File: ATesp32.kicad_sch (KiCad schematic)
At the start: 28 parts, among them SW1 SW_Push, SW2 SW_Push, U1 ESP32-S3, U2 ATmega32A-P, Y1 40 MHz

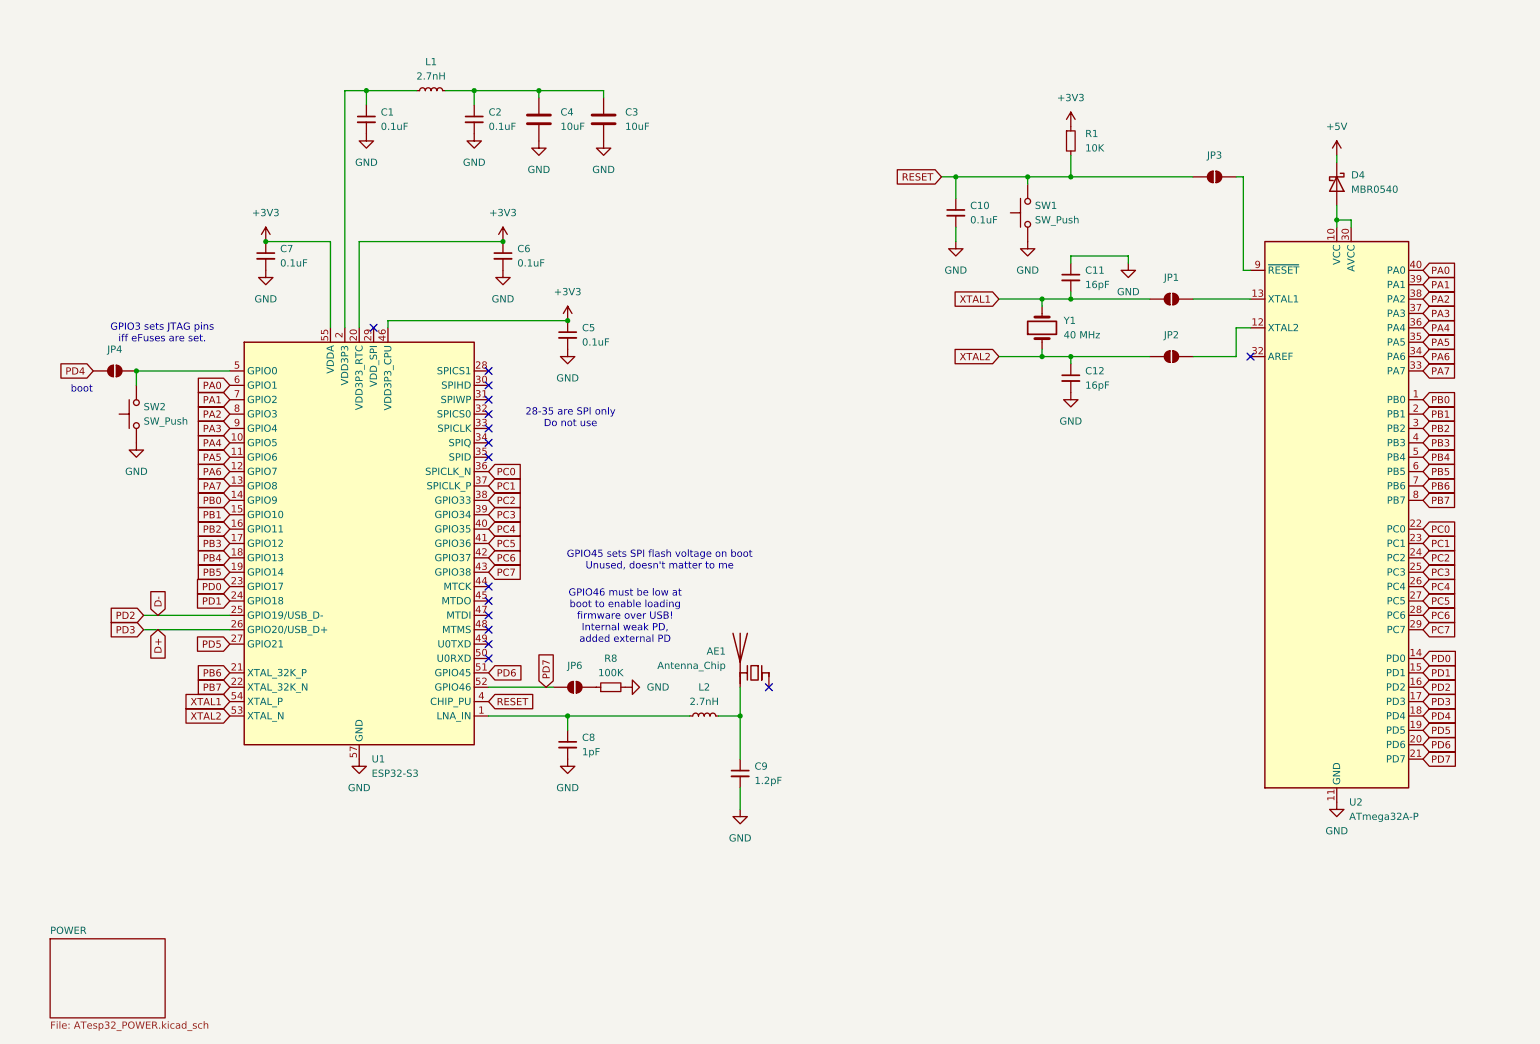
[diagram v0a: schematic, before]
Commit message: Added USB-UART bridge for programming
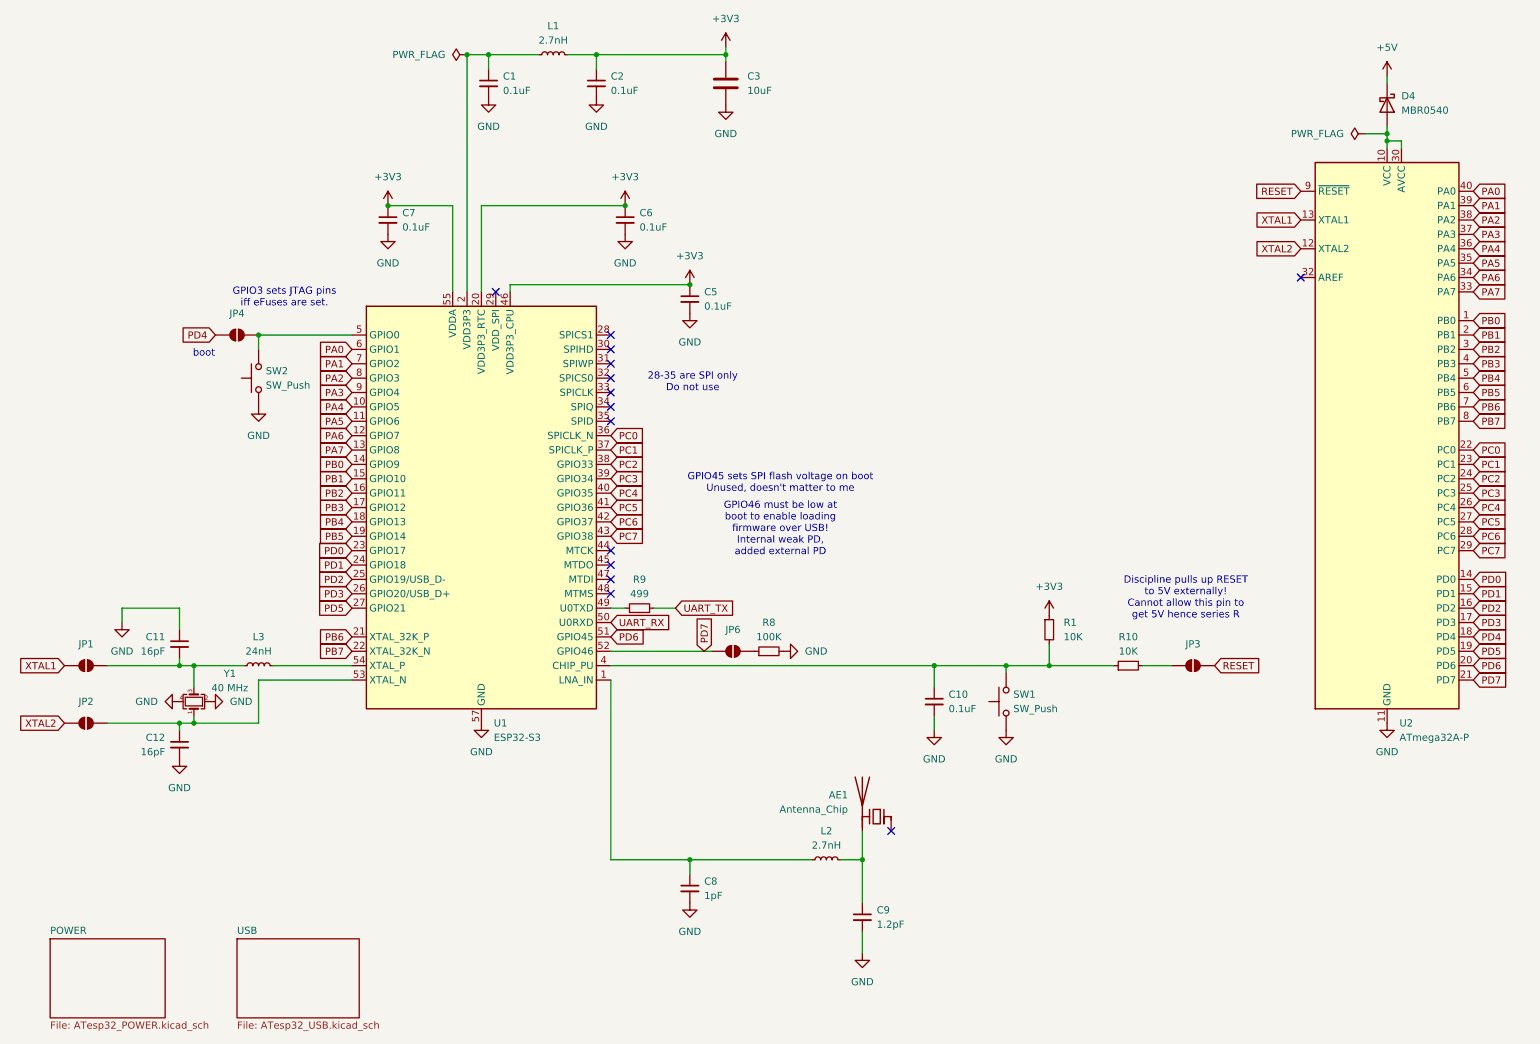
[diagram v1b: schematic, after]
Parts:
- removed C4: 10uF, symbol Device:C
- removed Y1: 40 MHz, symbol Device:Crystal
- added L3: 24nH, symbol Device:L_Small
- added R10: 10K, symbol Device:R_Small
- added R9: 499, symbol Device:R_Small
- added Y1: 40 MHz, symbol Device:Crystal_GND24_Small
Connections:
- net +3V3: now also C2.1, C3.1, L1.2
- net GND: now also Y1.2, Y1.4
- net RESET: now also JP3.2 (B), U2.9 (~{RESET}); no longer C10.1, JP3.1 (A), R1.2, SW1.2, U1.4 (CHIP_PU)
- net XTAL1: now also JP1.2 (B), U2.13 (XTAL1); no longer C11.2, JP1.1 (A), U1.54 (XTAL_P)
- net XTAL2: now also JP2.2 (B), U2.12 (XTAL2); no longer C12.1, JP2.1 (A), U1.53 (XTAL_N)
- net at U1.49 (U0TXD): now also R9.1
- net UART_RX: now reaches U1.50 (U0RXD)
- net D+ renamed PD3
- net D- renamed PD2
- new net: C12.1, JP2.1 (A), U1.53 (XTAL_N), Y1.1
- new net: C11.2, JP1.1 (A), L3.1, Y1.3
- new net: C10.1, R1.2, R10.1, SW1.2, U1.4 (CHIP_PU)
- new net: L3.2, U1.54 (XTAL_P)
- new net: JP3.1 (A), R10.2
- new net UART_TX: R9.2
- no-connect marks 16 -> 14
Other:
- added sheet USB (ATesp32_USB.kicad_sch)
- note added: "Discipline pulls up RESET to 5V externally! Cannot allow this pin to get 5V hence series R"
- moved on the sheet: AE1, C1, C10, C11, C12, C2, C3, C5, C6, C7, C8, C9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

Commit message: first pass at footprint assignment
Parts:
- AE1: footprint (none) -> RF_Antenna:Johanson_2450AT18x100
- C1, C10, C11, C12, C2, C3, C5, C6, C7, C8, C9: footprint (none) -> Capacitor_SMD:C_0603_1608Metric
- JP1, JP2, JP3, JP4, JP6: footprint (none) -> Jumper:SolderJumper-2_P1.3mm_Open_RoundedPad1.0x1.5mm
- L1, L2, L3: footprint (none) -> Inductor_SMD:L_0603_1608Metric
- R1, R10, R8, R9: footprint (none) -> Resistor_SMD:R_0603_1608Metric
- SW1, SW2: footprint (none) -> Button_Switch_SMD:SW_Push_1P1T_NO_CK_KMR2
- Y1: footprint (none) -> Crystal:Crystal_SMD_Abracon_ABM8G-4Pin_3.2x2.5mm
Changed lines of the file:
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@@
 			)
 		)
-		(property "Footprint" ""
+		(property "Footprint" "Capacitor_SMD:C_0603_1608Metric"
 			(at 135.89 63.5 0)
 			(effects
@@
 			)
 		)
-		(property "Footprint" ""
+		(property "Footprint" "RF_Antenna:Johanson_2450AT18x100"
 			(at 171.45 150.495 0)
 			(effects
@@
 			)
 		)
-		(property "Footprint" ""
+		(property "Footprint" "Crystal:Crystal_SMD_Abracon_ABM8G-4Pin_3.2x2.5mm"
 			(at 48.26 134.62 0)
 			(effects
@@
 			)
 		)
-		(property "Footprint" ""
+		(property "Footprint" "Jumper:SolderJumper-2_P1.3mm_Open_RoundedPad1.0x1.5mm"
 			(at 29.21 138.43 0)
 			(effects
@@
 			)
 		)
-		(property "Footprint" ""
+		(property "Footprint" "Capacitor_SMD:C_0603_1608Metric"
 			(at 119.38 25.4 0)
 			(effects
@@
 			)
 		)
-		(property "Footprint" ""
+		(property "Footprint" "Jumper:SolderJumper-2_P1.3mm_Open_RoundedPad1.0x1.5mm"
 			(at 29.21 128.27 0)
 			(effects
@@
 			)
 		)
-		(property "Footprint" ""
+		(property "Footprint" "Jumper:SolderJumper-2_P1.3mm_Open_RoundedPad1.0x1.5mm"
 			(at 143.51 125.73 0)
 			(effects
@@
 			)
 		)
-		(property "Footprint" ""
+		(property "Footprint" "Capacitor_SMD:C_0603_1608Metric"
 			(at 45.72 124.46 0)
 			(effects
@@
 			)
 		)
-		(property "Footprint" ""
+		(property "Footprint" "Capacitor_SMD:C_0603_1608Metric"
 			(at 166.37 172.72 0)
 			(effects
@@
 			)
 		)
-		(property "Footprint" ""
+		(property "Footprint" "Inductor_SMD:L_0603_1608Metric"
 			(at 111.76 20.32 0)
 			(effects
@@
 			)
 		)
-		(property "Footprint" ""
+		(property "Footprint" "Jumper:SolderJumper-2_P1.3mm_Open_RoundedPad1.0x1.5mm"
 			(at 224.79 128.27 0)
 			(effects
@@
 			)
 		)
-		(property "Footprint" ""
+		(property "Footprint" "Capacitor_SMD:C_0603_1608Metric"
 			(at 143.2052 29.21 0)
 			(effects
@@
 			)
 		)
-		(property "Footprint" ""
+		(property "Footprint" "Capacitor_SMD:C_0603_1608Metric"
 			(at 124.46 49.53 0)
 			(effects
@@
 			)
 		)
-		(property "Footprint" ""
+		(property "Footprint" "Capacitor_SMD:C_0603_1608Metric"
 			(at 100.33 25.4 0)
 			(effects
@@
 			)
 		)
-		(property "Footprint" ""
+		(property "Footprint" "Jumper:SolderJumper-2_P1.3mm_Open_RoundedPad1.0x1.5mm"
 			(at 55.88 69.85 0)
 			(effects
@@
 			)
 		)
-		(property "Footprint" ""
+		(property "Footprint" "Button_Switch_SMD:SW_Push_1P1T_NO_CK_KMR2"
 			(at 186.69 134.62 0)
 			(effects
@@
 			)
 		)
-		(property "Footprint" ""
+		(property "Footprint" "Capacitor_SMD:C_0603_1608Metric"
 			(at 82.55 49.53 0)
 			(effects
@@
 			)
 		)
-		(property "Footprint" ""
+		(property "Footprint" "Capacitor_SMD:C_0603_1608Metric"
 			(at 135.89 167.64 0)
 			(effects
@@
 			)
 		)
-		(property "Footprint" ""
+		(property "Footprint" "Resistor_SMD:R_0603_1608Metric"
 			(at 213.36 128.27 0)
 			(effects
@@
 			)
 		)
-		(property "Footprint" ""
+		(property "Footprint" "Capacitor_SMD:C_0603_1608Metric"
 			(at 45.72 142.24 0)
 			(effects
@@
 			)
 		)
-		(property "Footprint" ""
+		(property "Footprint" "Inductor_SMD:L_0603_1608Metric"
 			(at 59.69 128.27 0)
 			(effects
@@
 			)
 		)
-		(property "Footprint" ""
+		(property "Footprint" "Resistor_SMD:R_0603_1608Metric"
 			(at 149.86 125.73 0)
 			(effects
@@
 			)
 		)
-		(property "Footprint" ""
+		(property "Footprint" "Resistor_SMD:R_0603_1608Metric"
 			(at 127 118.11 0)
 			(effects
@@
 			)
 		)
-		(property "Footprint" ""
+		(property "Footprint" "Resistor_SMD:R_0603_1608Metric"
 			(at 199.39 121.92 0)
 			(effects
@@
 			)
 		)
-		(property "Footprint" ""
+		(property "Footprint" "Button_Switch_SMD:SW_Push_1P1T_NO_CK_KMR2"
 			(at 54.61 77.47 0)
 			(effects
@@
 			)
 		)
-		(property "Footprint" ""
+		(property "Footprint" "Capacitor_SMD:C_0603_1608Metric"
 			(at 179.07 134.62 0)
 			(effects
@@
 			)
 		)
-		(property "Footprint" ""
+		(property "Footprint" "Inductor_SMD:L_0603_1608Metric"
 			(at 160.02 162.56 0)
 			(effects

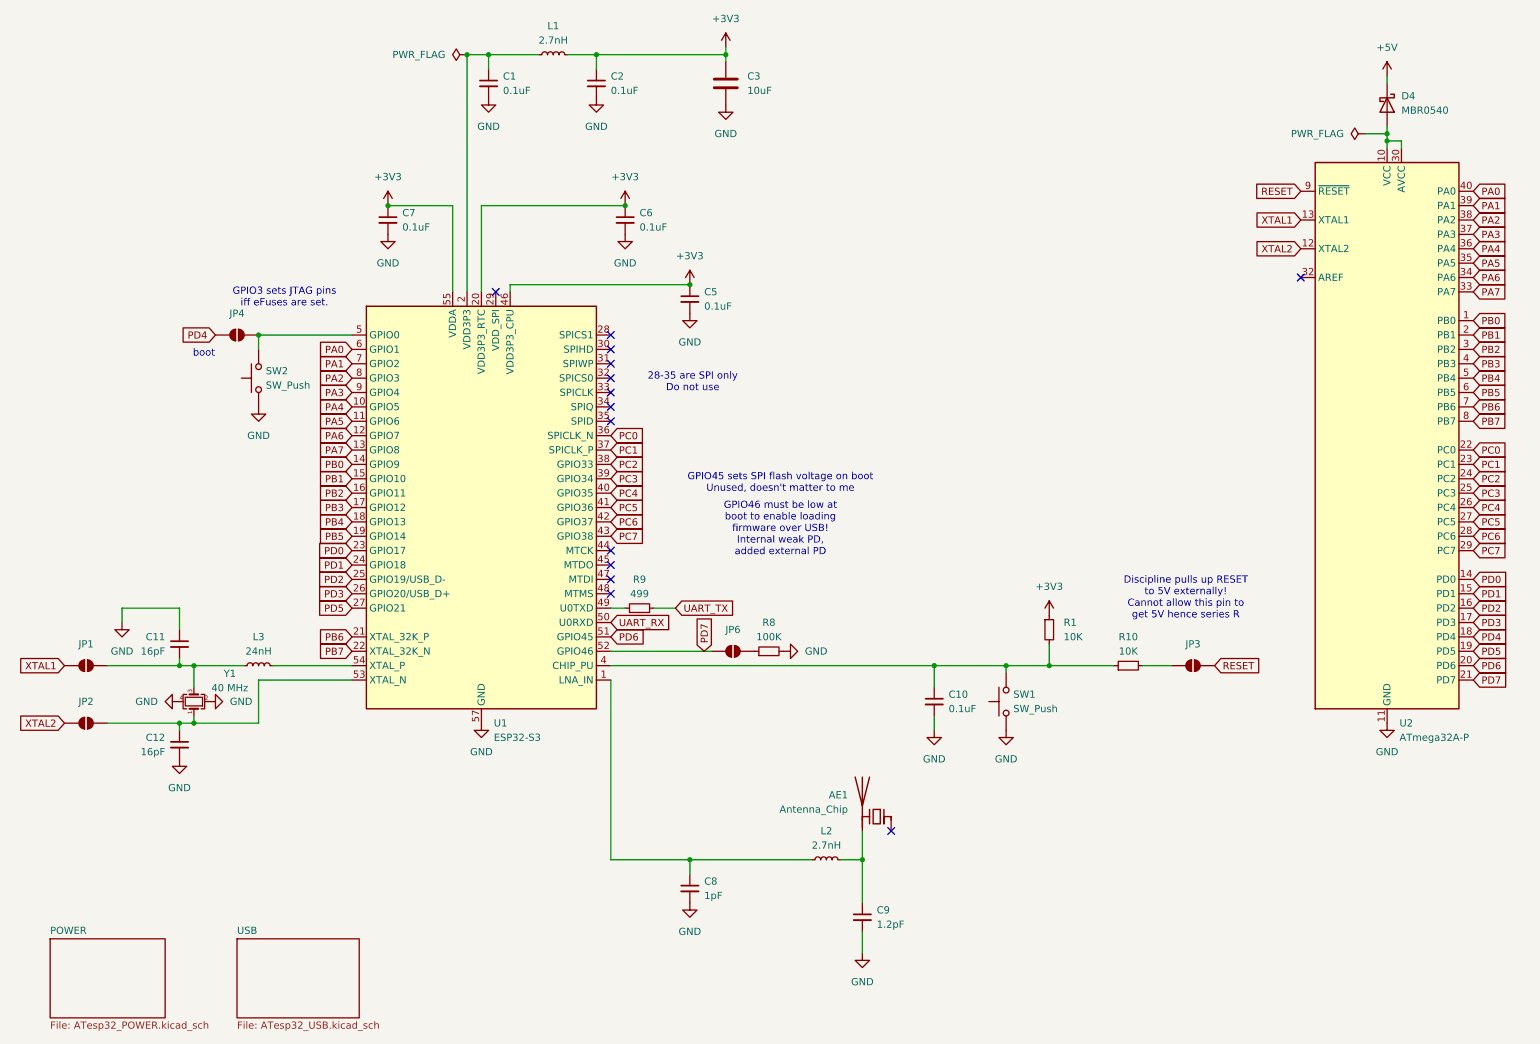
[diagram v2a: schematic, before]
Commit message: remove misc superfluous components
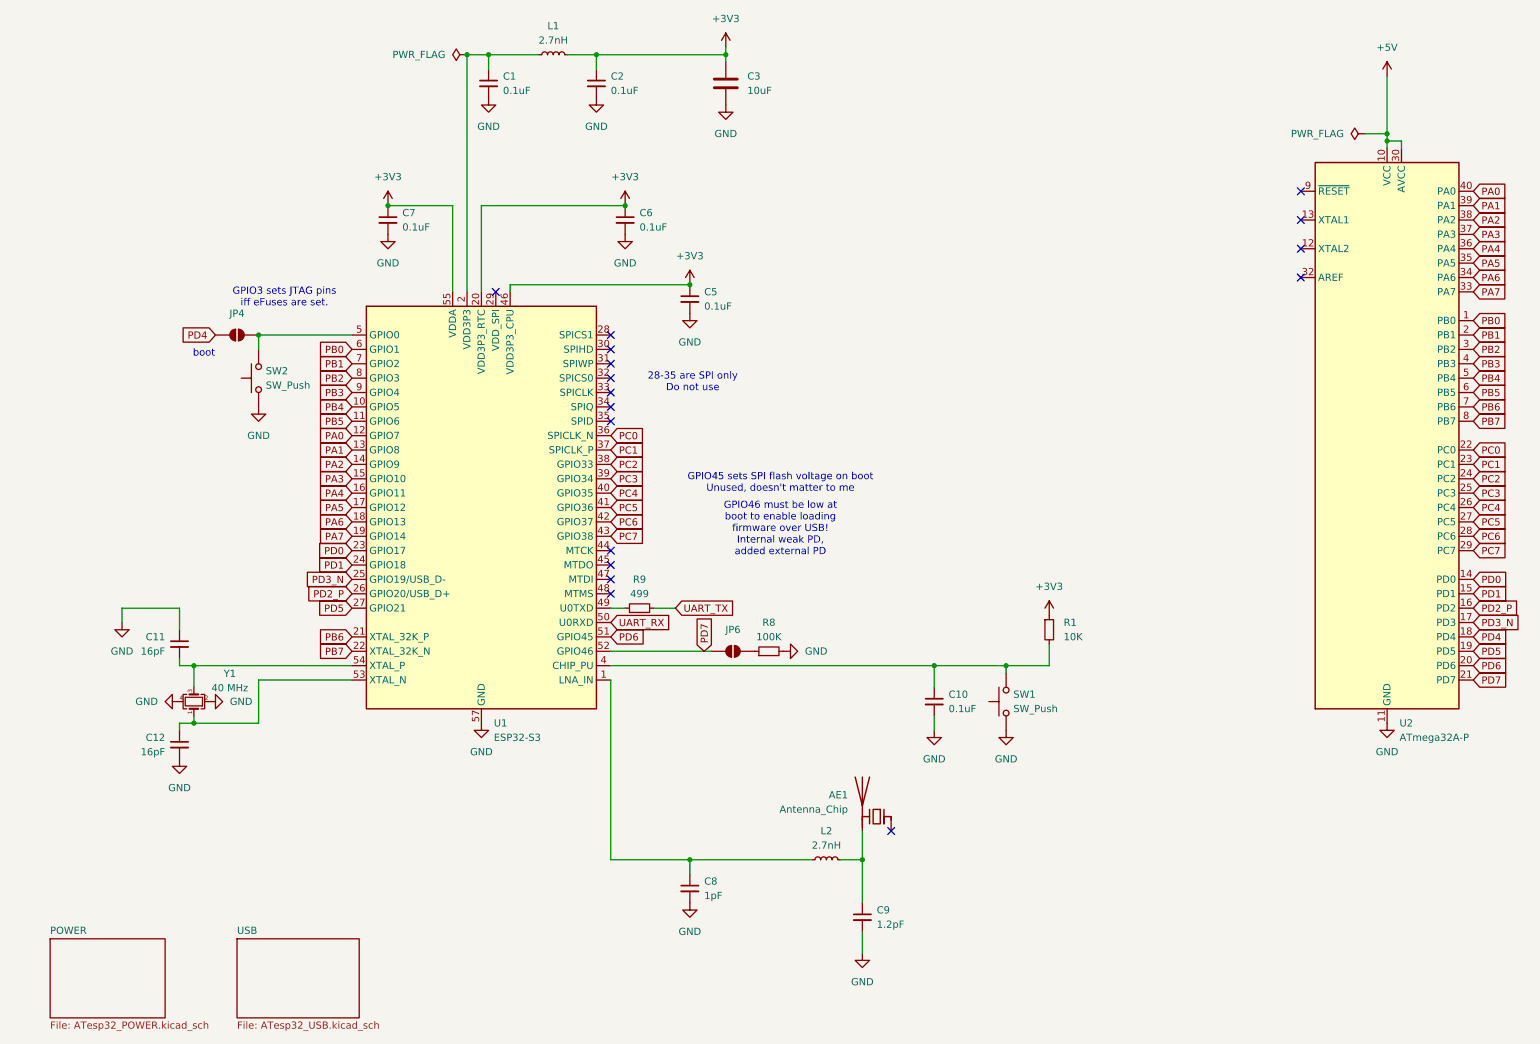
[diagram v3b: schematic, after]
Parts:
- removed D4: MBR0540, Diode_SMD:D_SOD-123, symbol Diode:MBR0540
- removed JP1, JP2, JP3: SolderJumper_2_Open, Jumper:SolderJumper-2_P1.3mm_Open_RoundedPad1.0x1.5mm, symbol Jumper:SolderJumper_2_Open
- removed L3: 24nH, Inductor_SMD:L_0603_1608Metric, symbol Device:L_Small
- removed R10: 10K, Resistor_SMD:R_0603_1608Metric, symbol Device:R_Small
- C1, C10, C2, C3, C5, C6, C7: footprint Capacitor_SMD:C_0603_1608Metric -> Capacitor_SMD:C_0402_1005Metric
- L1: DigiKey (none) -> 495-B82496C3279Z000CT-ND
- R1, R8, R9: footprint Resistor_SMD:R_0603_1608Metric -> Resistor_SMD:R_0402_1005Metric
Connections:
- net +5V: now also U2.10 (VCC), U2.30 (AVCC)
- net PA0: now also U1.12 (GPIO7); no longer U1.6 (GPIO1)
- net PA1: now also U1.13 (GPIO8); no longer U1.7 (GPIO2)
- net PA2: now also U1.14 (GPIO9); no longer U1.8 (GPIO3)
- net PA3: now also U1.15 (GPIO10); no longer U1.9 (GPIO4)
- net PA4: now also U1.16 (GPIO11); no longer U1.10 (GPIO5)
- net PA5: now also U1.17 (GPIO12); no longer U1.11 (GPIO6)
- net PA6: now also U1.18 (GPIO13); no longer U1.12 (GPIO7)
- net PA7: now also U1.19 (GPIO14); no longer U1.13 (GPIO8)
- net PB0: now also U1.6 (GPIO1); no longer U1.14 (GPIO9)
- net PB1: now also U1.7 (GPIO2); no longer U1.15 (GPIO10)
- net PB2: now also U1.8 (GPIO3); no longer U1.16 (GPIO11)
- net PB3: now also U1.9 (GPIO4); no longer U1.17 (GPIO12)
- net PB4: now also U1.10 (GPIO5); no longer U1.18 (GPIO13)
- net PB5: now also U1.11 (GPIO6); no longer U1.19 (GPIO14)
- net at C11.2, Y1.3: now also U1.54 (XTAL_P)
- net PD2 renamed PD2_P
- net PD2_P: now also U1.26 (GPIO20/USB_D+); no longer U1.25 (GPIO19/USB_D-)
- net PD3 renamed PD3_N
- net PD3_N: now also U1.25 (GPIO19/USB_D-); no longer U1.26 (GPIO20/USB_D+)
- net RESET: no longer names the net of U2.9 (~{RESET})
- net XTAL1: no longer names the net of U2.13 (XTAL1)
- net XTAL2: no longer names the net of U2.12 (XTAL2)
- no-connect marks 14 -> 17
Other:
- note removed: "Discipline pulls up RESET to 5V externally! Cannot allow this pin to get 5V hence series R"
